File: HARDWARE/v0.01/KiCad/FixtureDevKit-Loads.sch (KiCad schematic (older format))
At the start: 24 parts, among them J45 LOAD_0, J46 LOAD_1, J47 LOAD_2, J48 LOAD_3, Q1 NTF2955T1G, Q2 NTF2955T1G, Q3 NTF2955T1G, Q4 NTF2955T1G

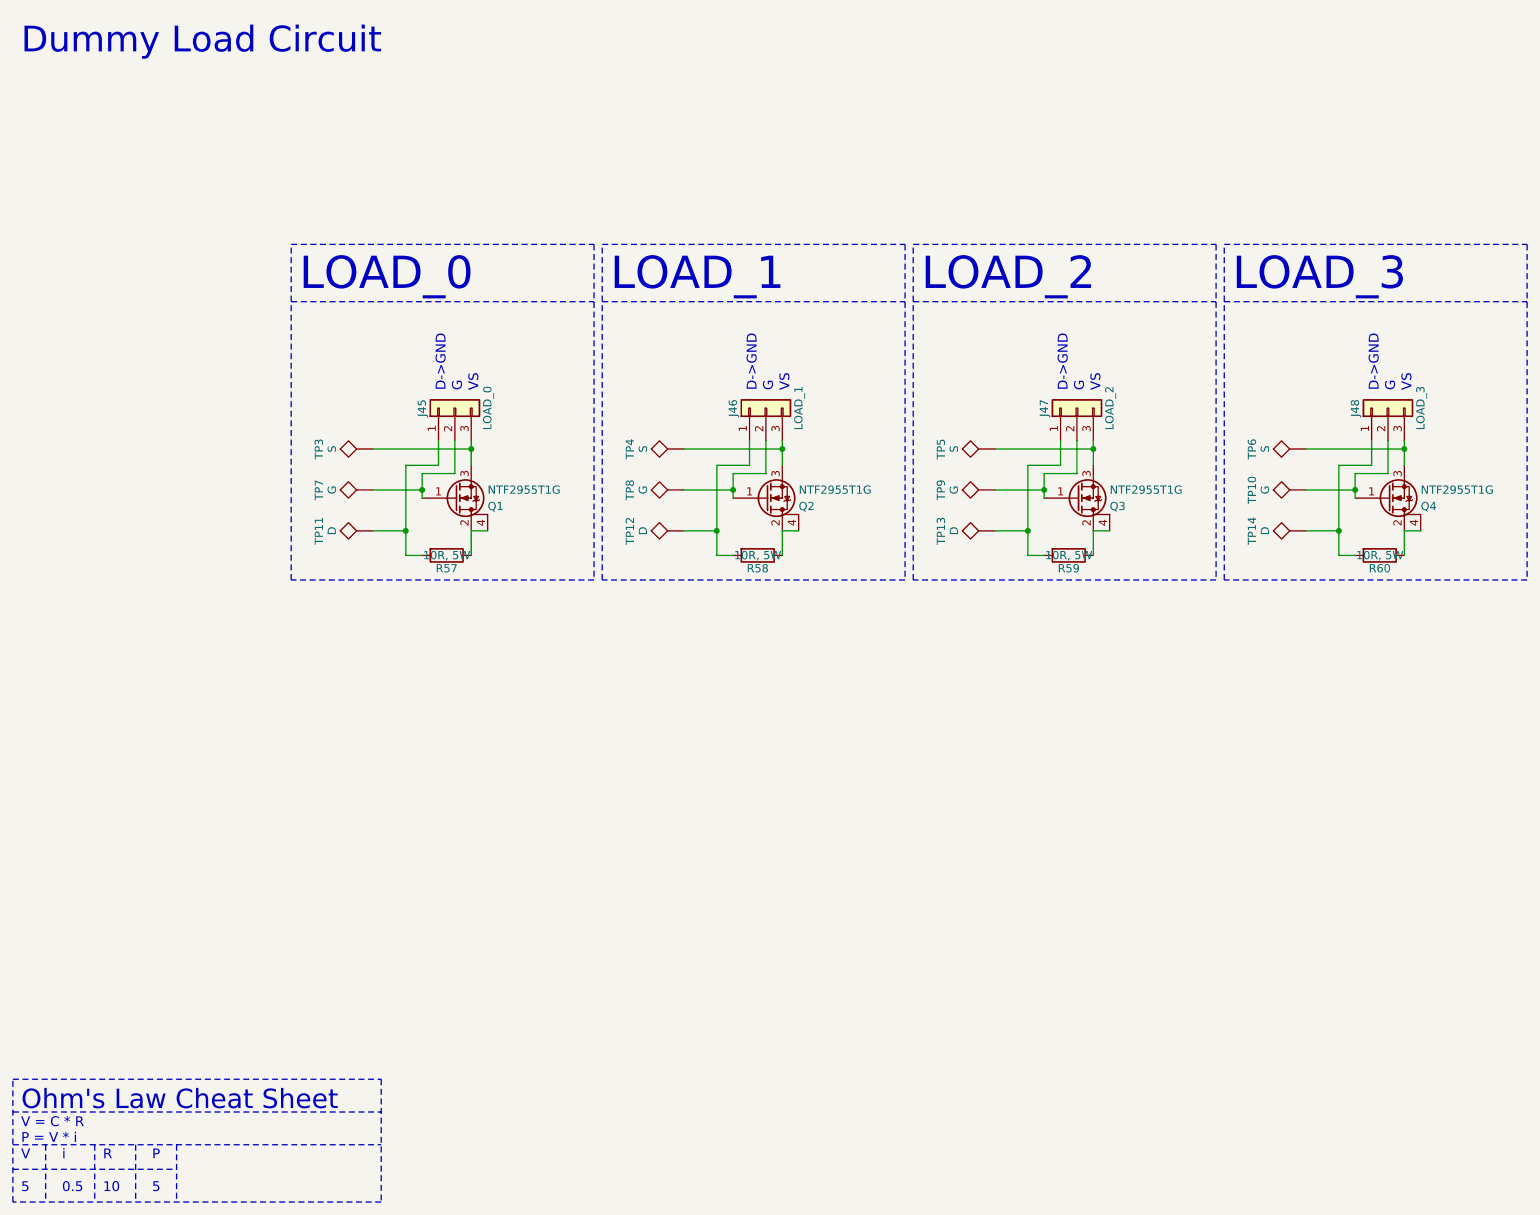
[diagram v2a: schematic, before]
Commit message: adjusting page sizes and cleaning up schematics
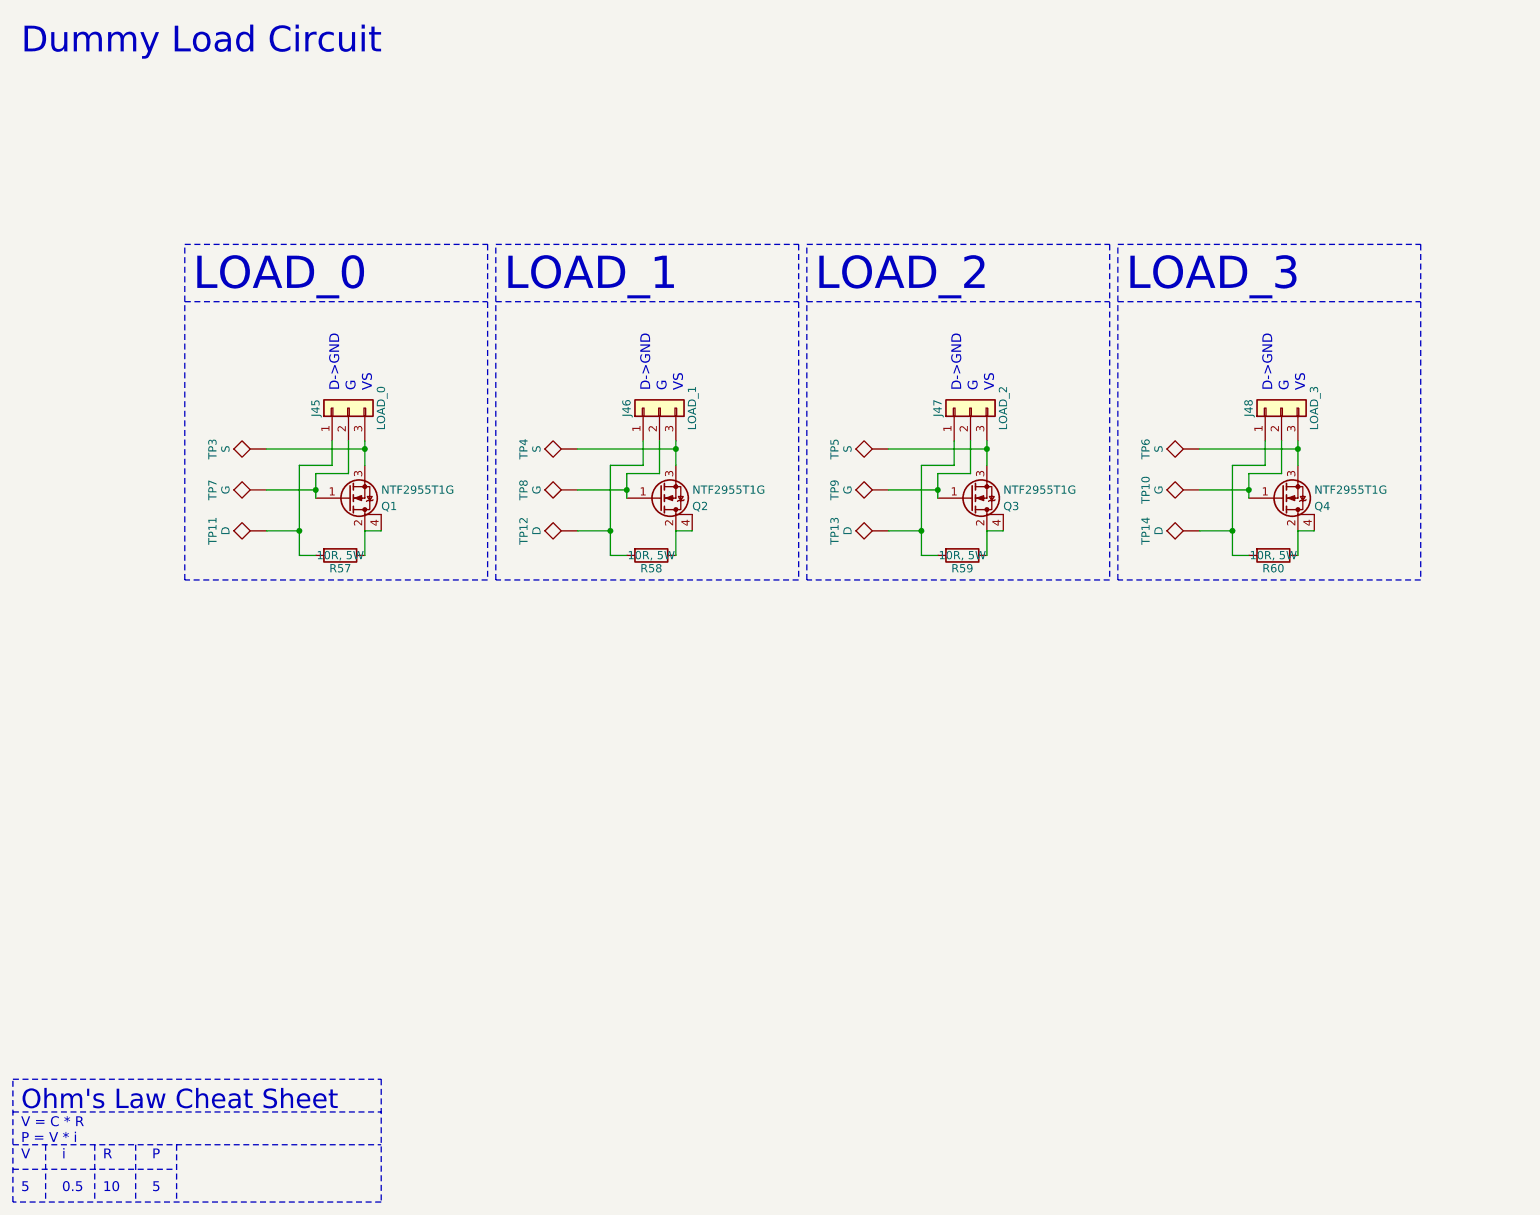
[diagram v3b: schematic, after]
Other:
- moved on the sheet: J45, J46, J47, J48, Q1, Q2, Q3, Q4, R57, R58, R59, R60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

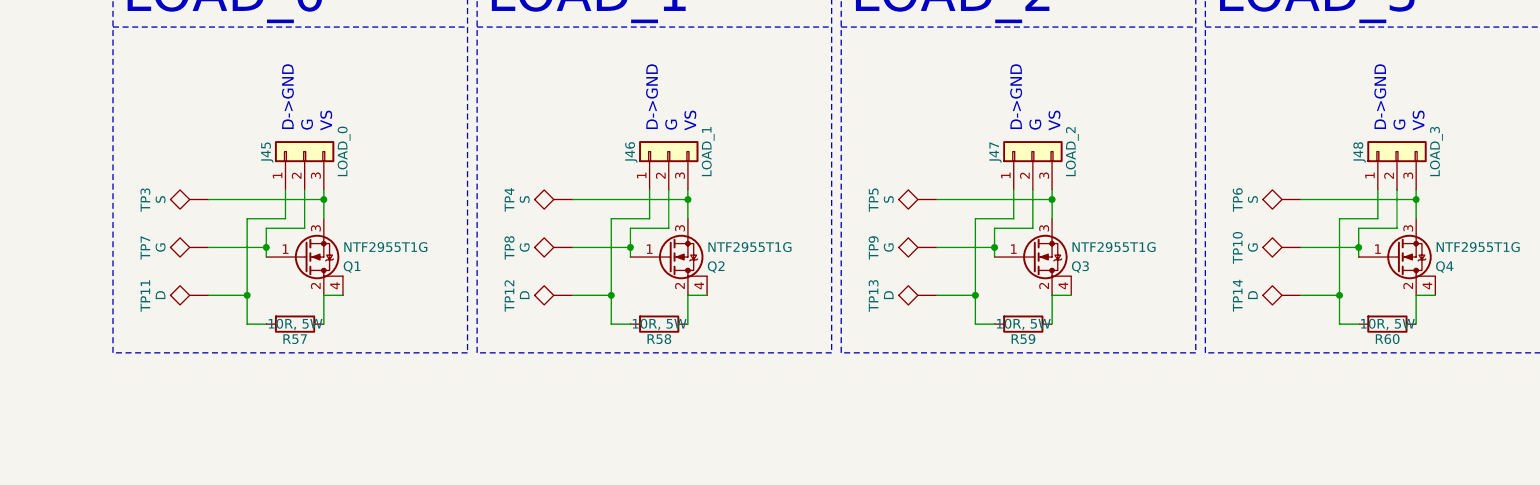
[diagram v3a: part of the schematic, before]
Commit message: cleaning up schematic, run rules check, generate net list
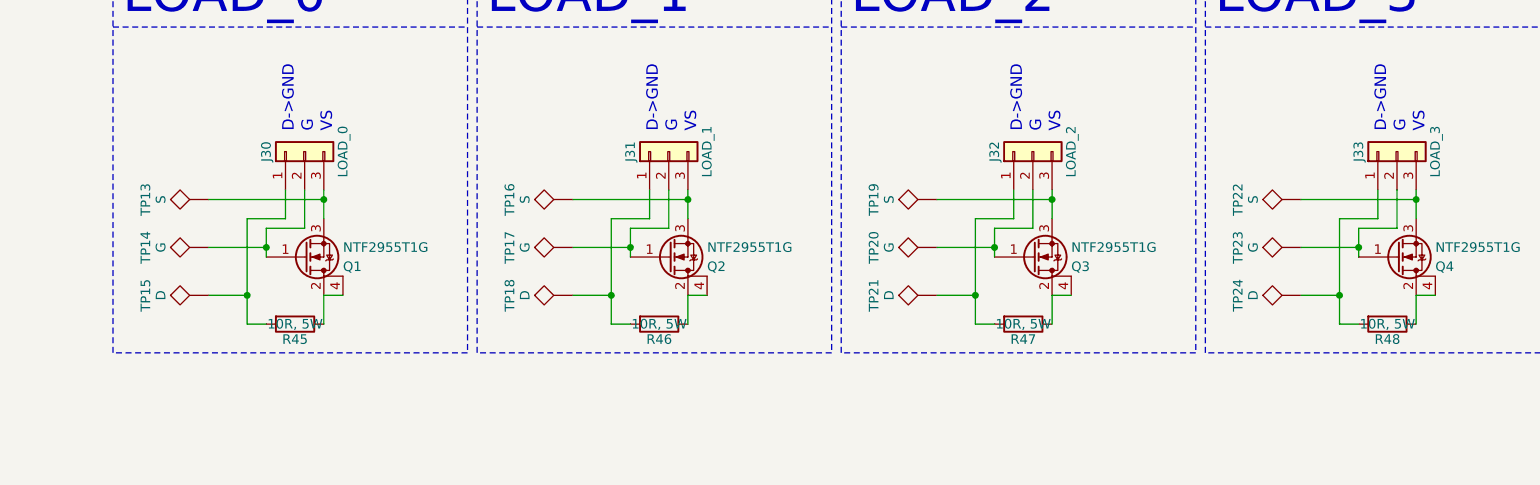
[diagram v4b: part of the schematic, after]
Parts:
- renumbered J45 to J30, J46 to J31, J47 to J32, J48 to J33, R57 to R45, R58 to R46, R59 to R47, R60 to R48, TP3 to TP13, TP7 to TP14, TP11 to TP15, TP4 to TP16, TP8 to TP17, TP12 to TP18, TP5 to TP19, TP9 to TP20, TP13 to TP21, TP6 to TP22, TP10 to TP23, TP14 to TP24
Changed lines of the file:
@@
 VS
 $Comp
-L R R57
+L R R45
 U 1 1 59EE69C1
 P 2500 3800
-F 0 "R57" V 2580 3800 50  0000 C CNN
+F 0 "R45" V 2580 3800 50  0000 C CNN
 F 1 "10R, 5W" V 2500 3800 50  0000 C CNN
 F 2 "" V 2430 3800 50  0001 C CNN
@@
 $EndComp
 $Comp
-L Conn_01x03 J45
+L Conn_01x03 J30
 U 1 1 59EE6A91
 P 2550 2900
-F 0 "J45" H 2550 3100 50  0000 C CNN
+F 0 "J30" H 2550 3100 50  0000 C CNN
 F 1 "LOAD_0" H 2550 2700 50  0000 C CNN
 F 2 "" H 2550 2900 50  0001 C CNN
@@
 	2550 3300 2550 3100
 $Comp
-L TEST TP3
+L TEST TP13
 U 1 1 59F066A1
 P 2050 3150
-F 0 "TP3" H 2050 3450 50  0000 C BNN
+F 0 "TP13" H 2050 3450 50  0000 C BNN
 F 1 "S" H 2050 3400 50  0000 C CNN
 F 2 "" H 2050 3150 50  0001 C CNN
@@
 $EndComp
 $Comp
-L TEST TP7
+L TEST TP14
 U 1 1 59F06708
 P 2050 3400
-F 0 "TP7" H 2050 3700 50  0000 C BNN
+F 0 "TP14" H 2050 3700 50  0000 C BNN
 F 1 "G" H 2050 3650 50  0000 C CNN
 F 2 "" H 2050 3400 50  0001 C CNN
@@
 $EndComp
 $Comp
-L TEST TP11
+L TEST TP15
 U 1 1 59F0672F
 P 2050 3650
-F 0 "TP11" H 2050 3950 50  0000 C BNN
+F 0 "TP15" H 2050 3950 50  0000 C BNN
 F 1 "D" H 2050 3900 50  0000 C CNN
 F 2 "" H 2050 3650 50  0001 C CNN
@@
 VS
 $Comp
-L R R58
+L R R46
 U 1 1 59F074EB
 P 4400 3800
-F 0 "R58" V 4480 3800 50  0000 C CNN
+F 0 "R46" V 4480 3800 50  0000 C CNN
 F 1 "10R, 5W" V 4400 3800 50  0000 C CNN
 F 2 "" V 4330 3800 50  0001 C CNN
@@
 $EndComp
 $Comp
-L Conn_01x03 J46
+L Conn_01x03 J31
 U 1 1 59F074F1
 P 4450 2900
-F 0 "J46" H 4450 3100 50  0000 C CNN
+F 0 "J31" H 4450 3100 50  0000 C CNN
 F 1 "LOAD_1" H 4450 2700 50  0000 C CNN
 F 2 "" H 4450 2900 50  0001 C CNN
@@
 	4450 3300 4450 3100
 $Comp
-L TEST TP4
+L TEST TP16
 U 1 1 59F07507
 P 3950 3150
-F 0 "TP4" H 3950 3450 50  0000 C BNN
+F 0 "TP16" H 3950 3450 50  0000 C BNN
 F 1 "S" H 3950 3400 50  0000 C CNN
 F 2 "" H 3950 3150 50  0001 C CNN
@@
 $EndComp
 $Comp
-L TEST TP8
+L TEST TP17
 U 1 1 59F0750D
 P 3950 3400
-F 0 "TP8" H 3950 3700 50  0000 C BNN
+F 0 "TP17" H 3950 3700 50  0000 C BNN
 F 1 "G" H 3950 3650 50  0000 C CNN
 F 2 "" H 3950 3400 50  0001 C CNN
@@
 $EndComp
 $Comp
-L TEST TP12
+L TEST TP18
 U 1 1 59F07513
 P 3950 3650
-F 0 "TP12" H 3950 3950 50  0000 C BNN
+F 0 "TP18" H 3950 3950 50  0000 C BNN
 F 1 "D" H 3950 3900 50  0000 C CNN
 F 2 "" H 3950 3650 50  0001 C CNN
@@
 VS
 $Comp
-L R R59
+L R R47
 U 1 1 59F07D08
 P 6300 3800
-F 0 "R59" V 6380 3800 50  0000 C CNN
+F 0 "R47" V 6380 3800 50  0000 C CNN
 F 1 "10R, 5W" V 6300 3800 50  0000 C CNN
 F 2 "" V 6230 3800 50  0001 C CNN
@@
 $EndComp
 $Comp
-L Conn_01x03 J47
+L Conn_01x03 J32
 U 1 1 59F07D0E
 P 6350 2900
-F 0 "J47" H 6350 3100 50  0000 C CNN
+F 0 "J32" H 6350 3100 50  0000 C CNN
 F 1 "LOAD_2" H 6350 2700 50  0000 C CNN
 F 2 "" H 6350 2900 50  0001 C CNN
@@
 	6350 3300 6350 3100
 $Comp
-L TEST TP5
+L TEST TP19
 U 1 1 59F07D24
 P 5850 3150
-F 0 "TP5" H 5850 3450 50  0000 C BNN
+F 0 "TP19" H 5850 3450 50  0000 C BNN
 F 1 "S" H 5850 3400 50  0000 C CNN
 F 2 "" H 5850 3150 50  0001 C CNN
@@
 $EndComp
 $Comp
-L TEST TP9
+L TEST TP20
 U 1 1 59F07D2A
 P 5850 3400
-F 0 "TP9" H 5850 3700 50  0000 C BNN
+F 0 "TP20" H 5850 3700 50  0000 C BNN
 F 1 "G" H 5850 3650 50  0000 C CNN
 F 2 "" H 5850 3400 50  0001 C CNN
@@
 $EndComp
 $Comp
-L TEST TP13
+L TEST TP21
 U 1 1 59F07D30
 P 5850 3650
-F 0 "TP13" H 5850 3950 50  0000 C BNN
+F 0 "TP21" H 5850 3950 50  0000 C BNN
 F 1 "D" H 5850 3900 50  0000 C CNN
 F 2 "" H 5850 3650 50  0001 C CNN
@@
 VS
 $Comp
-L R R60
+L R R48
 U 1 1 59F07D45
 P 8200 3800
-F 0 "R60" V 8280 3800 50  0000 C CNN
+F 0 "R48" V 8280 3800 50  0000 C CNN
 F 1 "10R, 5W" V 8200 3800 50  0000 C CNN
 F 2 "" V 8130 3800 50  0001 C CNN
@@
 $EndComp
 $Comp
-L Conn_01x03 J48
+L Conn_01x03 J33
 U 1 1 59F07D4B
 P 8250 2900
-F 0 "J48" H 8250 3100 50  0000 C CNN
+F 0 "J33" H 8250 3100 50  0000 C CNN
 F 1 "LOAD_3" H 8250 2700 50  0000 C CNN
 F 2 "" H 8250 2900 50  0001 C CNN
@@
 	8250 3300 8250 3100
 $Comp
-L TEST TP6
+L TEST TP22
 U 1 1 59F07D61
 P 7750 3150
-F 0 "TP6" H 7750 3450 50  0000 C BNN
+F 0 "TP22" H 7750 3450 50  0000 C BNN
 F 1 "S" H 7750 3400 50  0000 C CNN
 F 2 "" H 7750 3150 50  0001 C CNN
@@
 $EndComp
 $Comp
-L TEST TP10
+L TEST TP23
 U 1 1 59F07D67
 P 7750 3400
-F 0 "TP10" H 7750 3700 50  0000 C BNN
+F 0 "TP23" H 7750 3700 50  0000 C BNN
 F 1 "G" H 7750 3650 50  0000 C CNN
 F 2 "" H 7750 3400 50  0001 C CNN
@@
 $EndComp
 $Comp
-L TEST TP14
+L TEST TP24
 U 1 1 59F07D6D
 P 7750 3650
-F 0 "TP14" H 7750 3950 50  0000 C BNN
+F 0 "TP24" H 7750 3950 50  0000 C BNN
 F 1 "D" H 7750 3900 50  0000 C CNN
 F 2 "" H 7750 3650 50  0001 C CNN

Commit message: adding footprints
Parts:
- J30, J31, J32, J33: footprint (none) -> Pin_Headers:Pin_Header_Straight_1x03_Pitch2.54mm
- Q1, Q2, Q3, Q4: footprint (none) -> Pin_Headers:Pin_Header_Straight_1x04_Pitch2.54mm
- R45: footprint (none) -> Resistors_SMD:R_0805_HandSoldering
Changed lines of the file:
@@
 F 0 "R45" V 2580 3800 50  0000 C CNN
 F 1 "10R, 5W" V 2500 3800 50  0000 C CNN
-F 2 "" V 2430 3800 50  0001 C CNN
+F 2 "Resistors_SMD:R_0805_HandSoldering" V 2430 3800 50  0001 C CNN
 F 3 "" H 2500 3800 50  0001 C CNN
 	1    2500 3800
@@
 F 0 "J30" H 2550 3100 50  0000 C CNN
 F 1 "LOAD_0" H 2550 2700 50  0000 C CNN
-F 2 "" H 2550 2900 50  0001 C CNN
+F 2 "Pin_Headers:Pin_Header_Straight_1x03_Pitch2.54mm" H 2550 2900 50  0001 C CNN
 F 3 "" H 2550 2900 50  0001 C CNN
 	1    2550 2900
@@
 F 0 "Q1" H 2750 3500 50  0000 L CNN
 F 1 "NTF2955T1G" H 2750 3400 50  0000 L CNN
-F 2 "" H 2750 3550 50  0001 C CNN
+F 2 "Pin_Headers:Pin_Header_Straight_1x04_Pitch2.54mm" H 2750 3550 50  0001 C CNN
 F 3 "" H 2550 3450 50  0001 C CNN
 	1    2550 3450
@@
 F 0 "J31" H 4450 3100 50  0000 C CNN
 F 1 "LOAD_1" H 4450 2700 50  0000 C CNN
-F 2 "" H 4450 2900 50  0001 C CNN
+F 2 "Pin_Headers:Pin_Header_Straight_1x03_Pitch2.54mm" H 4450 2900 50  0001 C CNN
 F 3 "" H 4450 2900 50  0001 C CNN
 	1    4450 2900
@@
 F 0 "Q2" H 4650 3500 50  0000 L CNN
 F 1 "NTF2955T1G" H 4650 3400 50  0000 L CNN
-F 2 "" H 4650 3550 50  0001 C CNN
+F 2 "Pin_Headers:Pin_Header_Straight_1x04_Pitch2.54mm" H 4650 3550 50  0001 C CNN
 F 3 "" H 4450 3450 50  0001 C CNN
 	1    4450 3450
@@
 F 0 "J32" H 6350 3100 50  0000 C CNN
 F 1 "LOAD_2" H 6350 2700 50  0000 C CNN
-F 2 "" H 6350 2900 50  0001 C CNN
+F 2 "Pin_Headers:Pin_Header_Straight_1x03_Pitch2.54mm" H 6350 2900 50  0001 C CNN
 F 3 "" H 6350 2900 50  0001 C CNN
 	1    6350 2900
@@
 F 0 "Q3" H 6550 3500 50  0000 L CNN
 F 1 "NTF2955T1G" H 6550 3400 50  0000 L CNN
-F 2 "" H 6550 3550 50  0001 C CNN
+F 2 "Pin_Headers:Pin_Header_Straight_1x04_Pitch2.54mm" H 6550 3550 50  0001 C CNN
 F 3 "" H 6350 3450 50  0001 C CNN
 	1    6350 3450
@@
 F 0 "J33" H 8250 3100 50  0000 C CNN
 F 1 "LOAD_3" H 8250 2700 50  0000 C CNN
-F 2 "" H 8250 2900 50  0001 C CNN
+F 2 "Pin_Headers:Pin_Header_Straight_1x03_Pitch2.54mm" H 8250 2900 50  0001 C CNN
 F 3 "" H 8250 2900 50  0001 C CNN
 	1    8250 2900
@@
 F 0 "Q4" H 8450 3500 50  0000 L CNN
 F 1 "NTF2955T1G" H 8450 3400 50  0000 L CNN
-F 2 "" H 8450 3550 50  0001 C CNN
+F 2 "Pin_Headers:Pin_Header_Straight_1x04_Pitch2.54mm" H 8450 3550 50  0001 C CNN
 F 3 "" H 8250 3450 50  0001 C CNN
 	1    8250 3450

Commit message: adding footprints, starting layout
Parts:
- Q1, Q2, Q3, Q4: footprint Pin_Headers:Pin_Header_Straight_1x04_Pitch2.54mm -> TO_SOT_Packages_SMD:SOT-223
- TP13, TP14, TP15, TP16, TP17, TP18, TP19, TP20, TP21, TP22, TP23, TP24: footprint (none) -> TestPoint:TestPoint
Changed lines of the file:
@@
 LIBS:contrib
 LIBS:valves
-LIBS:FDN337N
+LIBS:TCA6424ARGJR
 LIBS:Fixture-Dev-Kit-cache
 EELAYER 25 0
@@
 F 0 "Q1" H 2750 3500 50  0000 L CNN
 F 1 "NTF2955T1G" H 2750 3400 50  0000 L CNN
-F 2 "Pin_Headers:Pin_Header_Straight_1x04_Pitch2.54mm" H 2750 3550 50  0001 C CNN
+F 2 "TO_SOT_Packages_SMD:SOT-223" H 2750 3550 50  0001 C CNN
 F 3 "" H 2550 3450 50  0001 C CNN
 	1    2550 3450
@@
 F 0 "TP13" H 2050 3450 50  0000 C BNN
 F 1 "S" H 2050 3400 50  0000 C CNN
-F 2 "" H 2050 3150 50  0001 C CNN
+F 2 "TestPoint:TestPoint" H 2050 3150 50  0001 C CNN
 F 3 "" H 2050 3150 50  0001 C CNN
 	1    2050 3150
@@
 F 0 "TP14" H 2050 3700 50  0000 C BNN
 F 1 "G" H 2050 3650 50  0000 C CNN
-F 2 "" H 2050 3400 50  0001 C CNN
+F 2 "TestPoint:TestPoint" H 2050 3400 50  0001 C CNN
 F 3 "" H 2050 3400 50  0001 C CNN
 	1    2050 3400
@@
 F 0 "TP15" H 2050 3950 50  0000 C BNN
 F 1 "D" H 2050 3900 50  0000 C CNN
-F 2 "" H 2050 3650 50  0001 C CNN
+F 2 "TestPoint:TestPoint" H 2050 3650 50  0001 C CNN
 F 3 "" H 2050 3650 50  0001 C CNN
 	1    2050 3650
@@
 F 0 "Q2" H 4650 3500 50  0000 L CNN
 F 1 "NTF2955T1G" H 4650 3400 50  0000 L CNN
-F 2 "Pin_Headers:Pin_Header_Straight_1x04_Pitch2.54mm" H 4650 3550 50  0001 C CNN
+F 2 "TO_SOT_Packages_SMD:SOT-223" H 4650 3550 50  0001 C CNN
 F 3 "" H 4450 3450 50  0001 C CNN
 	1    4450 3450
@@
 F 0 "TP16" H 3950 3450 50  0000 C BNN
 F 1 "S" H 3950 3400 50  0000 C CNN
-F 2 "" H 3950 3150 50  0001 C CNN
+F 2 "TestPoint:TestPoint" H 3950 3150 50  0001 C CNN
 F 3 "" H 3950 3150 50  0001 C CNN
 	1    3950 3150
@@
 F 0 "TP17" H 3950 3700 50  0000 C BNN
 F 1 "G" H 3950 3650 50  0000 C CNN
-F 2 "" H 3950 3400 50  0001 C CNN
+F 2 "TestPoint:TestPoint" H 3950 3400 50  0001 C CNN
 F 3 "" H 3950 3400 50  0001 C CNN
 	1    3950 3400
@@
 F 0 "TP18" H 3950 3950 50  0000 C BNN
 F 1 "D" H 3950 3900 50  0000 C CNN
-F 2 "" H 3950 3650 50  0001 C CNN
+F 2 "TestPoint:TestPoint" H 3950 3650 50  0001 C CNN
 F 3 "" H 3950 3650 50  0001 C CNN
 	1    3950 3650
@@
 F 0 "Q3" H 6550 3500 50  0000 L CNN
 F 1 "NTF2955T1G" H 6550 3400 50  0000 L CNN
-F 2 "Pin_Headers:Pin_Header_Straight_1x04_Pitch2.54mm" H 6550 3550 50  0001 C CNN
+F 2 "TO_SOT_Packages_SMD:SOT-223" H 6550 3550 50  0001 C CNN
 F 3 "" H 6350 3450 50  0001 C CNN
 	1    6350 3450
@@
 F 0 "TP19" H 5850 3450 50  0000 C BNN
 F 1 "S" H 5850 3400 50  0000 C CNN
-F 2 "" H 5850 3150 50  0001 C CNN
+F 2 "TestPoint:TestPoint" H 5850 3150 50  0001 C CNN
 F 3 "" H 5850 3150 50  0001 C CNN
 	1    5850 3150
@@
 F 0 "TP20" H 5850 3700 50  0000 C BNN
 F 1 "G" H 5850 3650 50  0000 C CNN
-F 2 "" H 5850 3400 50  0001 C CNN
+F 2 "TestPoint:TestPoint" H 5850 3400 50  0001 C CNN
 F 3 "" H 5850 3400 50  0001 C CNN
 	1    5850 3400
@@
 F 0 "TP21" H 5850 3950 50  0000 C BNN
 F 1 "D" H 5850 3900 50  0000 C CNN
-F 2 "" H 5850 3650 50  0001 C CNN
+F 2 "TestPoint:TestPoint" H 5850 3650 50  0001 C CNN
 F 3 "" H 5850 3650 50  0001 C CNN
 	1    5850 3650
@@
 F 0 "Q4" H 8450 3500 50  0000 L CNN
 F 1 "NTF2955T1G" H 8450 3400 50  0000 L CNN
-F 2 "Pin_Headers:Pin_Header_Straight_1x04_Pitch2.54mm" H 8450 3550 50  0001 C CNN
+F 2 "TO_SOT_Packages_SMD:SOT-223" H 8450 3550 50  0001 C CNN
 F 3 "" H 8250 3450 50  0001 C CNN
 	1    8250 3450
@@
 F 0 "TP22" H 7750 3450 50  0000 C BNN
 F 1 "S" H 7750 3400 50  0000 C CNN
-F 2 "" H 7750 3150 50  0001 C CNN
+F 2 "TestPoint:TestPoint" H 7750 3150 50  0001 C CNN
 F 3 "" H 7750 3150 50  0001 C CNN
 	1    7750 3150
@@
 F 0 "TP23" H 7750 3700 50  0000 C BNN
 F 1 "G" H 7750 3650 50  0000 C CNN
-F 2 "" H 7750 3400 50  0001 C CNN
+F 2 "TestPoint:TestPoint" H 7750 3400 50  0001 C CNN
 F 3 "" H 7750 3400 50  0001 C CNN
 	1    7750 3400
@@
 F 0 "TP24" H 7750 3950 50  0000 C BNN
 F 1 "D" H 7750 3900 50  0000 C CNN
-F 2 "" H 7750 3650 50  0001 C CNN
+F 2 "TestPoint:TestPoint" H 7750 3650 50  0001 C CNN
 F 3 "" H 7750 3650 50  0001 C CNN
 	1    7750 3650
